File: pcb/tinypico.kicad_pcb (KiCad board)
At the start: 2 copper layers, 19 x 14.1 mm, 9 parts, among them J1 Conn_01x05_Pin, J2 Conn_01x05_Pin, U1 ATtiny202-SS

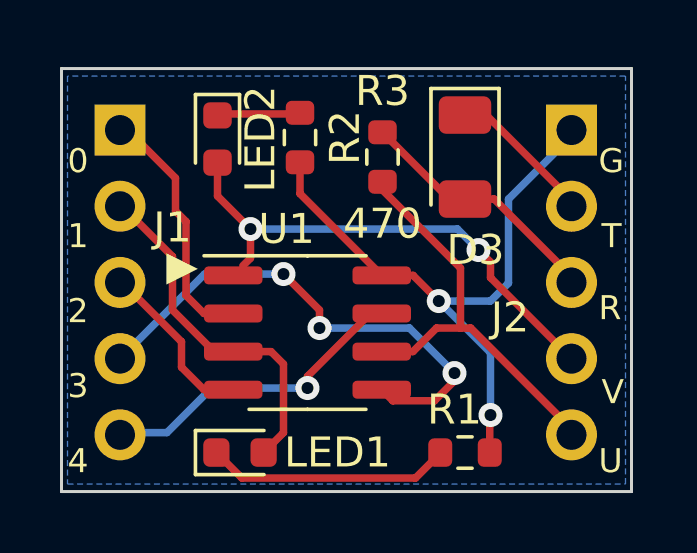
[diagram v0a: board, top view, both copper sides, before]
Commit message: RXとTXを入れ替え。他リファクタリング。
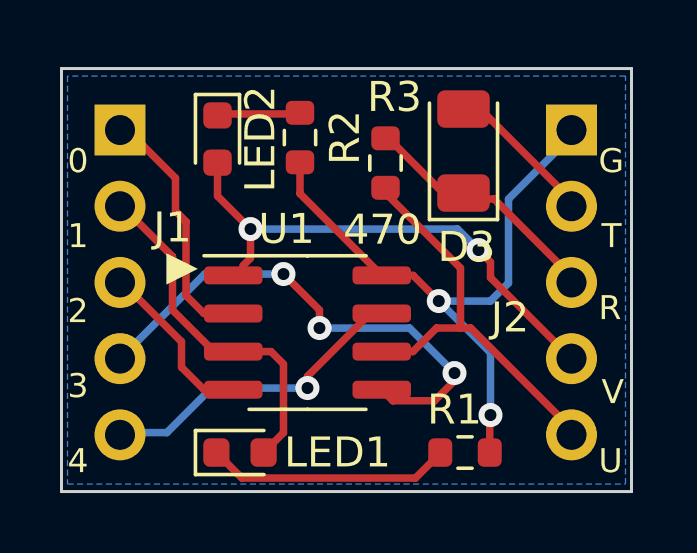
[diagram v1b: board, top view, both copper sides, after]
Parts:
- moved 470 0.22 mm to (96.6, 74.1)
- moved D3 0.21 mm to (99.2, 73.7), turned to 90 degrees
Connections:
- D3 pad 1: UPDI_TX -> UPDI_RX
- D3 pad 2: UPDI_RX -> UPDI_TX
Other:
- board text added: "GND"
- board text added: "UPDI"
- board text added: "UPDI_RX"
- board text added: "UPDI_TX"
- board text added: "VCC"
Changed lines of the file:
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@@
 (kicad_pcb (version 20221018) (generator pcbnew)
   (general
-    (thickness 1.6)
+    (thickness 1.4)
   )
   (paper "A4")
@@
   )
   (setup
+    (stackup
+      (layer "F.SilkS" (type "Top Silk Screen"))
+      (layer "F.Paste" (type "Top Solder Paste"))
+      (layer "F.Mask" (type "Top Solder Mask") (thickness 0.01))
+      (layer "F.Cu" (type "copper") (thickness 0.035))
+      (layer "dielectric 1" (type "core") (thickness 1.31) (material "FR4") (epsilon_r 4.5) (loss_tangent 0.02))
+      (layer "B.Cu" (type "copper") (thickness 0.035))
+      (layer "B.Mask" (type "Bottom Solder Mask") (thickness 0.01))
+      (layer "B.Paste" (type "Bottom Solder Paste"))
+      (layer "B.SilkS" (type "Bottom Silk Screen"))
+      (copper_finish "None")
+      (dielectric_constraints no)
+    )
     (pad_to_mask_clearance 0)
     (pcbplotparams
@@
   (net 12 "UPDI_TX")
   (footprint "Resistor_SMD:R_0603_1608Metric" (layer "F.Cu")
-    (at 96.5 73.9 90)
+    (at 96.6 74.1 90)
     (descr "Resistor SMD 0603 (1608 Metric), square (rectangular) end terminal, IPC_7351 nominal, (Body size source: IPC-SM-782 page 72, https://www.pcb-3d.com/wordpress/wp-content/uploads/ipc-sm-782a_amendment_1_and_2.pdf), generated with kicad-footprint-generator")
     (tags "resistor")
@@
     (property "ki_keywords" "R res resistor")
     (attr smd)
-    (fp_text reference "470" (at -2.225 0) (layer "F.SilkS")
-        (effects (font (size 1 1) (thickness 0.15)))
-    )
-    (fp_text value "R3" (at 2.2 0) (layer "F.SilkS")
+    (fp_text reference "470" (at -2.225 -0.1) (layer "F.SilkS")
+        (effects (font (size 1 1) (thickness 0.15)))
+    )
+    (fp_text value "R3" (at 2.2 0.3) (layer "F.SilkS")
         (effects (font (size 1 1) (thickness 0.15)))
     )
@@
   )
   (footprint "Diode_SMD:D_1206_3216Metric" (layer "F.Cu")
-    (at 99.25 73.9 -90)
+    (at 99.2 73.7 90)
     (descr "Diode SMD 1206 (3216 Metric), square (rectangular) end terminal, IPC_7351 nominal, (Body size source: http://www.tortai-tech.com/upload/download/2011102023233369053.pdf), generated with kicad-footprint-generator")
     (tags "diode")
@@
     (property "ki_keywords" "diode")
     (attr smd)
-    (fp_text reference "D3" (at 3.1 -0.35) (layer "F.SilkS")
-        (effects (font (size 1 1) (thickness 0.15)))
-    )
-    (fp_text value "RB160M-30" (at -3.9 -2.75) (layer "F.Fab")
+    (fp_text reference "D3" (at -3.2 0.1) (layer "F.SilkS")
+        (effects (font (size 1 1) (thickness 0.15)))
+    )
+    (fp_text value "RB160M-30" (at 4.8 1.65) (layer "F.Fab")
         (effects (font (size 1 1) (thickness 0.15)))
     )
@@
     (fp_line (start 1.6 0.8) (end 1.6 -0.8)
       (stroke (width 0.1) (type solid)) (layer "F.Fab"))
-    (pad "1" smd roundrect (at -1.4 0 270) (size 1.25 1.75) (layers "F.Cu" "F.Paste" "F.Mask") (roundrect_rratio 0.2)
-      (net 12 "UPDI_TX") (pinfunction "K") (pintype "passive"))
-    (pad "2" smd roundrect (at 1.4 0 270) (size 1.25 1.75) (layers "F.Cu" "F.Paste" "F.Mask") (roundrect_rratio 0.2)
-      (net 11 "UPDI_RX") (pinfunction "A") (pintype "passive"))
+    (pad "1" smd roundrect (at -1.4 0 90) (size 1.25 1.75) (layers "F.Cu" "F.Paste" "F.Mask") (roundrect_rratio 0.2)
+      (net 11 "UPDI_RX") (pinfunction "K") (pintype "passive"))
+    (pad "2" smd roundrect (at 1.4 0 90) (size 1.25 1.75) (layers "F.Cu" "F.Paste" "F.Mask") (roundrect_rratio 0.2)
+      (net 12 "UPDI_TX") (pinfunction "A") (pintype "passive"))
     (model "${KICAD6_3DMODEL_DIR}/Diode_SMD.3dshapes/D_1206_3216Metric.wrl"
       (offset (xyz 0 0 0))
@@
   (gr_rect (start 85.8 70.95) (end 104.8 85.05)
     (stroke (width 0.1) (type default)) (fill none) (layer "Edge.Cuts"))
-  (gr_text "G" (at 101.47 74.48) (layer "B.SilkS")
-    (effects (font (size 0.8 0.8) (thickness 0.1875)) (justify left bottom mirror))
-  )
-  (gr_text "V" (at 101.37 82.18) (layer "B.SilkS")
+  (gr_text "GND" (at 101.47 74.48) (layer "B.SilkS")
+    (effects (font (size 0.8 0.8) (thickness 0.1875)) (justify left bottom mirror))
+  )
+  (gr_text "VCC" (at 101.37 82.18) (layer "B.SilkS")
     (effects (font (size 0.8 0.8) (thickness 0.1875)) (justify left bottom mirror))
   )
@@
     (effects (font (size 0.8 0.8) (thickness 0.1875)) (justify left bottom mirror))
   )
-  (gr_text "R" (at 101.47 79.38) (layer "B.SilkS")
+  (gr_text "UPDI_RX" (at 101.47 79.38) (layer "B.SilkS")
     (effects (font (size 0.8 0.8) (thickness 0.1875)) (justify left bottom mirror))
   )
@@
     (effects (font (size 0.8 0.8) (thickness 0.1875)) (justify left bottom mirror))
   )
-  (gr_text "T" (at 101.37 76.98) (layer "B.SilkS")
-    (effects (font (size 0.8 0.8) (thickness 0.1875)) (justify left bottom mirror))
-  )
-  (gr_text "U" (at 101.47 84.48) (layer "B.SilkS")
-    (effects (font (size 0.8 0.8) (thickness 0.1875)) (justify left bottom mirror))
-  )
+  (gr_text "UPDI_TX" (at 101.37 76.98) (layer "B.SilkS")
+    (effects (font (size 0.8 0.8) (thickness 0.1875)) (justify left bottom mirror))
+  )
+  (gr_text "UPDI" (at 101.47 84.48) (layer "B.SilkS")
+    (effects (font (size 0.8 0.8) (thickness 0.1875)) (justify left bottom mirror))
+  )
